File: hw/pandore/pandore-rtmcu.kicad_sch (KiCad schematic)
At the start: 0 parts

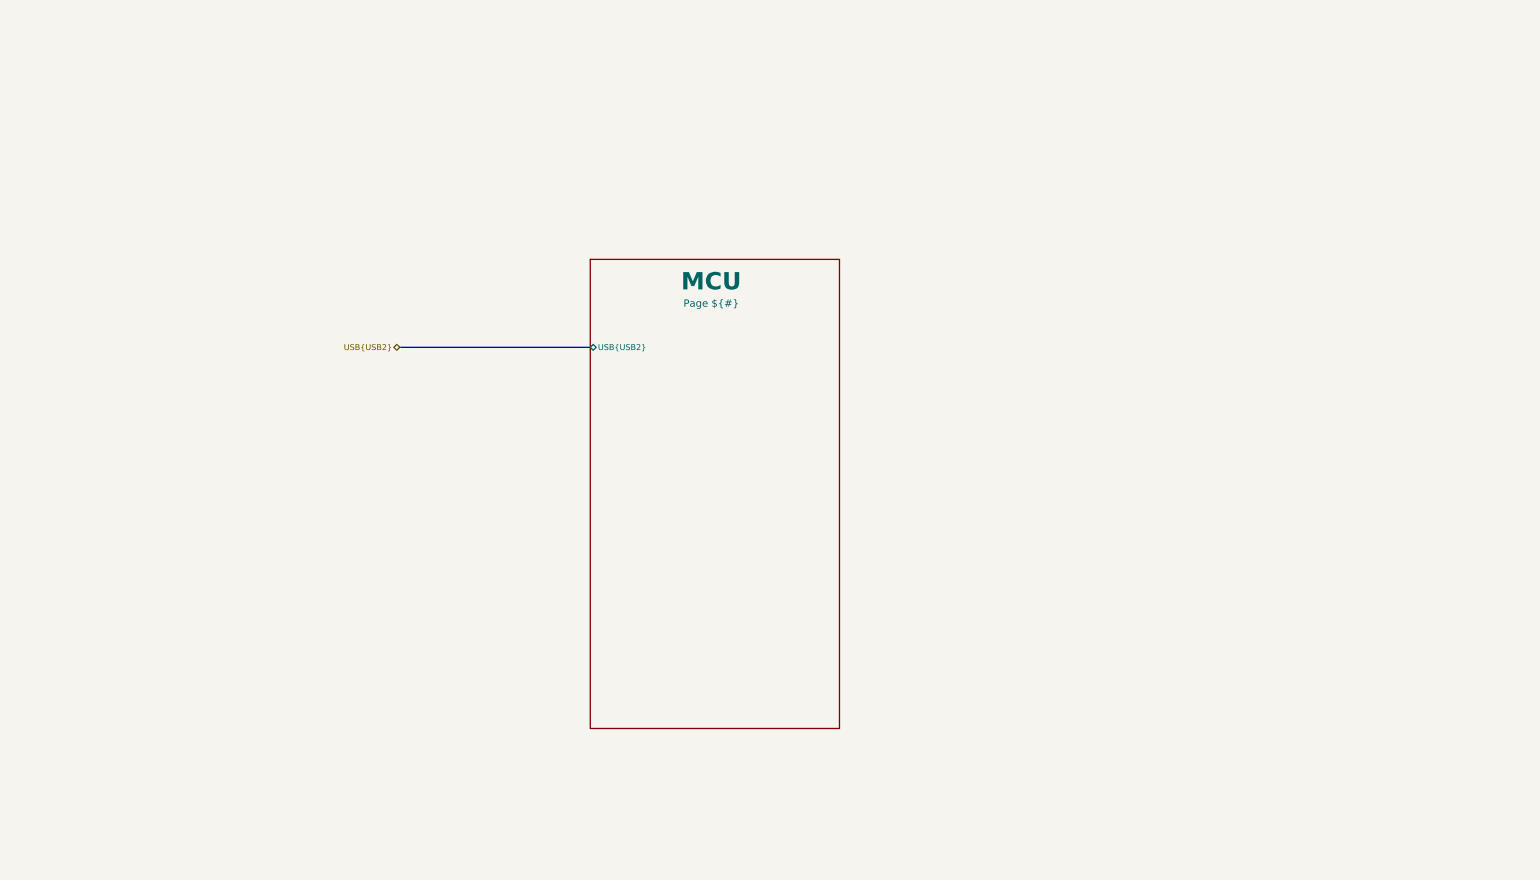
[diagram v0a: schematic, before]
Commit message: Added lots to sch and pcb: eth passive, audio codec, midi, teensy Corrected and added support for M.2
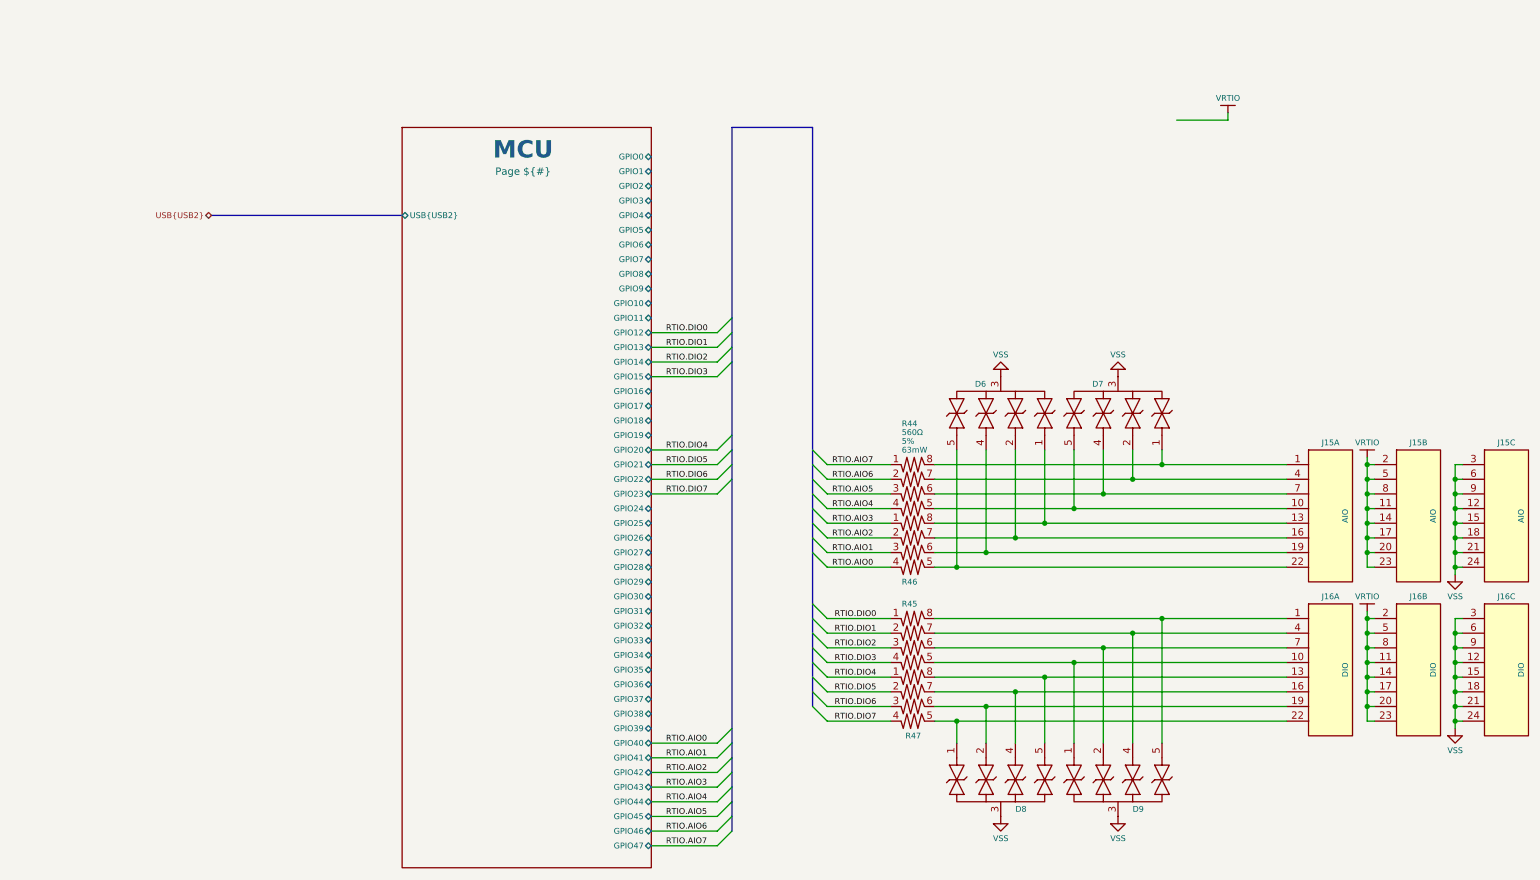
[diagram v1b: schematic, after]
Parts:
- added D6, D7, D8, D9: ${Vbr}, reekilib_dfn:DFN50P100X250X55-10, symbol reekilib_tvs:diode_tvsbi_4
- added J15: AIO, reekilib_con:HDR254P3X8-THRA, symbol reekilib_con:hdr-3x8
- added J16: DIO, reekilib_con:HDR254P3X8-THRA, symbol reekilib_con:hdr-3x8
- added R44, R45, R46, R47: ${Resistance}, ${Tolerance}, ${Power}, reekilib_res:RESCAXSR50P200X100X35-8, symbol reekilib_res:res_4
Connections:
- new net: D8.1, J16.22, R47.5
- new net: D8.2, J16.19, R47.6
- new net: D8.4, J16.16, R47.7
- new net: D8.5, J16.13, R47.8
- new net: D7.1, J15.1, R44.8
- new net: D7.5, J15.10, R44.5
- new net: D6.1, J15.13, R46.8
- new net: D6.2, J15.16, R46.7
- new net: D6.4, J15.19, R46.6
- new net: D6.5, J15.22, R46.5
- new net: D7.2, J15.4, R44.7
- new net: D7.4, J15.7, R44.6
- new net: D9.5, J16.1, R45.8
- new net: D9.1, J16.10, R45.5
- new net: D9.4, J16.4, R45.7
- new net: D9.2, J16.7, R45.6
- new net RTIO.AIO0: R46.4
- new net RTIO.AIO1: R46.3
- new net RTIO.AIO2: R46.2
- new net RTIO.AIO3: R46.1
- new net RTIO.AIO4: R44.4
- new net RTIO.AIO5: R44.3
- new net RTIO.AIO6: R44.2
- new net RTIO.AIO7: R44.1
- new net RTIO.DIO0: R45.1
- new net RTIO.DIO1: R45.2
- new net RTIO.DIO2: R45.3
- new net RTIO.DIO3: R45.4
- new net RTIO.DIO4: R47.1
- new net RTIO.DIO5: R47.2
- new net RTIO.DIO6: R47.3
- new net RTIO.DIO7: R47.4
- new net VRTIO: J15.11, J15.14, J15.17, J15.2, J15.20, J15.23, J15.5, J15.8, J16.11, J16.14, J16.17, J16.2, J16.20, J16.23, J16.5, J16.8
- new net VSS: D6.3, D7.3, D8.3, D9.3, J15.12, J15.15, J15.18, J15.21, J15.24, J15.3, J15.6, J15.9, J16.12, J16.15, J16.18, J16.21, J16.24, J16.3, J16.6, J16.9
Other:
- sheet MCU ports: added GPIO0, GPIO1, GPIO10, GPIO11, GPIO12, GPIO13, GPIO14, GPIO15, GPIO16, GPIO17, GPIO18, GPIO19, GPIO2, GPIO20, GPIO21, GPIO22, GPIO23, GPIO24, GPIO25, GPIO26, GPIO27, GPIO28, GPIO29, GPIO3, GPIO30, GPIO31, GPIO32, GPIO33, GPIO34, GPIO35, GPIO36, GPIO37, GPIO38, GPIO39, GPIO4, GPIO40, GPIO41, GPIO42, GPIO43, GPIO44, GPIO45, GPIO46, GPIO47, GPIO5, GPIO6, GPIO7, GPIO8, GPIO9; removed none

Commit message: Lots of routing done power blocks intra-routing mostly done rp2350 routing mostly done some label cleanup
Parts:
- D6, D7, D8, D9: footprint reekilib_dfn:DFN50P100X250X55-10 -> reekilib_dfn:DFN50P100X250X55-10_ESD204
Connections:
- net RTIO.DIO0: now also R47.4; no longer R45.1
- net RTIO.DIO1: now also R47.3; no longer R45.2
- net RTIO.DIO2: now also R47.2; no longer R45.3
- net RTIO.DIO3: now also R47.1; no longer R45.4
- net RTIO.DIO4: now also R45.4; no longer R47.1
- net RTIO.DIO5: now also R45.3; no longer R47.2
- net RTIO.DIO6: now also R45.2; no longer R47.3
- net RTIO.DIO7: now also R45.1; no longer R47.4
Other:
- sheet MCU ports: added VIO; removed none

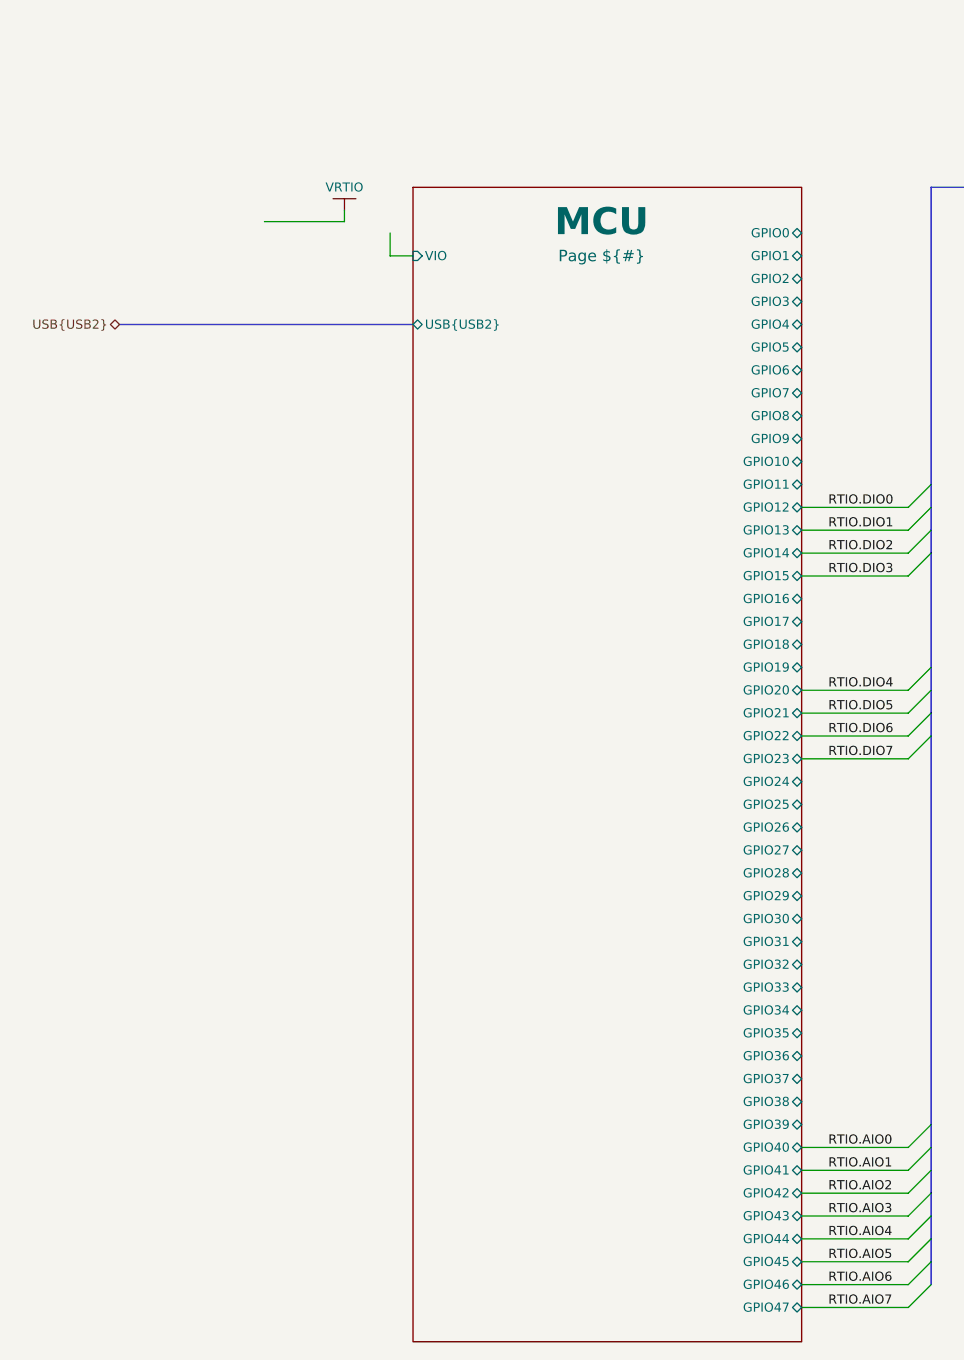
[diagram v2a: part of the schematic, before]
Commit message: added encoder, more routing done, pinout doc added
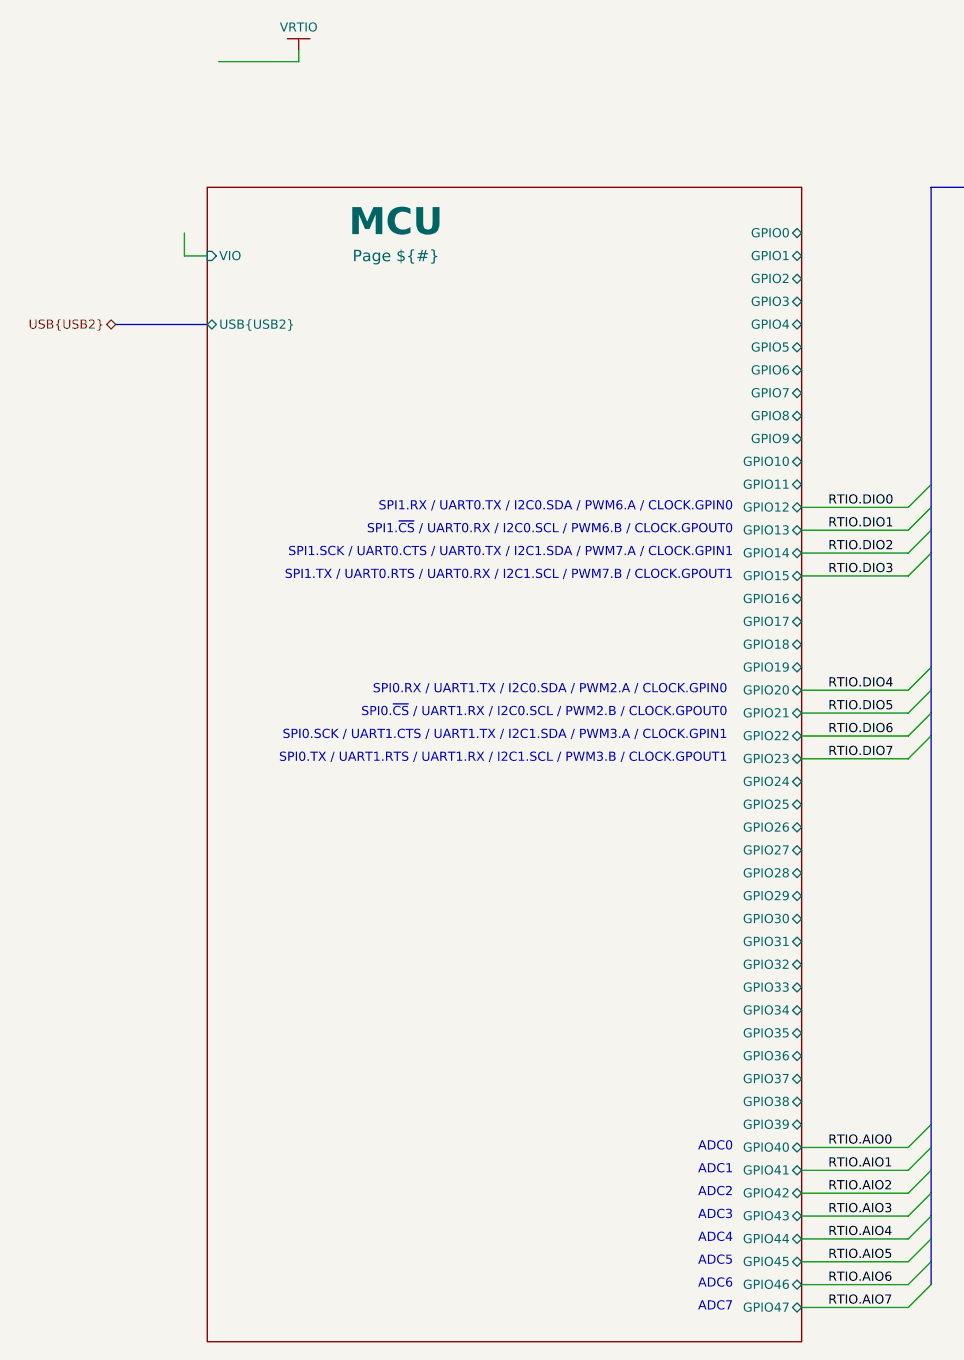
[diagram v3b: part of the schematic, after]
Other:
- note added: "ADC0"
- note added: "ADC1"
- note added: "ADC2"
- note added: "ADC3"
- note added: "ADC4"
- note added: "ADC5"
- note added: "ADC6"
- note added: "ADC7"
- note added: "SPI0.RX / UART1.TX / I2C0.SDA / PWM2.A / CLOCK.GPIN0"
- note added: "SPI0.SCK / UART1.CTS / UART1.TX / I2C1.SDA / PWM3.A / CLOCK.GPIN1"
- note added: "SPI0.TX / UART1.RTS / UART1.RX / I2C1.SCL / PWM3.B / CLOCK.GPOUT1"
- note added: "SPI0.~{CS} / UART1.RX / I2C0.SCL / PWM2.B / CLOCK.GPOUT0"
- note added: "SPI1.RX / UART0.TX / I2C0.SDA / PWM6.A / CLOCK.GPIN0"
- note added: "SPI1.SCK / UART0.CTS / UART0.TX / I2C1.SDA / PWM7.A / CLOCK.GPIN1"
- note added: "SPI1.TX / UART0.RTS / UART0.RX / I2C1.SCL / PWM7.B / CLOCK.GPOUT1"
- note added: "SPI1.~{CS} / UART0.RX / I2C0.SCL / PWM6.B / CLOCK.GPOUT0"
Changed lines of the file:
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@@
 		(company "${corp}")
 	)
+	(text "ADC1"
+		(exclude_from_sim no)
+		(at 121.92 147.32 0)
+		(effects
+			(font
+				(size 1.016 1.016)
+			)
+			(justify right)
+		)
+	)
+	(text "SPI0.~{CS} / UART1.RX / I2C0.SCL / PWM2.B / CLOCK.GPOUT0"
+		(exclude_from_sim no)
+		(at 121.285 96.52 0)
+		(effects
+			(font
+				(size 1.016 1.016)
+			)
+			(justify right)
+		)
+	)
+	(text "ADC6"
+		(exclude_from_sim no)
+		(at 121.92 160.02 0)
+		(effects
+			(font
+				(size 1.016 1.016)
+			)
+			(justify right)
+		)
+	)
+	(text "SPI0.RX / UART1.TX / I2C0.SDA / PWM2.A / CLOCK.GPIN0"
+		(exclude_from_sim no)
+		(at 121.285 93.98 0)
+		(effects
+			(font
+				(size 1.016 1.016)
+			)
+			(justify right)
+		)
+	)
+	(text "SPI1.SCK / UART0.CTS / UART0.TX / I2C1.SDA / PWM7.A / CLOCK.GPIN1"
+		(exclude_from_sim no)
+		(at 121.92 78.74 0)
+		(effects
+			(font
+				(size 1.016 1.016)
+			)
+			(justify right)
+		)
+	)
+	(text "SPI0.TX / UART1.RTS / UART1.RX / I2C1.SCL / PWM3.B / CLOCK.GPOUT1"
+		(exclude_from_sim no)
+		(at 121.285 101.6 0)
+		(effects
+			(font
+				(size 1.016 1.016)
+			)
+			(justify right)
+		)
+	)
+	(text "SPI1.~{CS} / UART0.RX / I2C0.SCL / PWM6.B / CLOCK.GPOUT0"
+		(exclude_from_sim no)
+		(at 121.92 76.2 0)
+		(effects
+			(font
+				(size 1.016 1.016)
+			)
+			(justify right)
+		)
+	)
+	(text "SPI0.SCK / UART1.CTS / UART1.TX / I2C1.SDA / PWM3.A / CLOCK.GPIN1"
+		(exclude_from_sim no)
+		(at 121.285 99.06 0)
+		(effects
+			(font
+				(size 1.016 1.016)
+			)
+			(justify right)
+		)
+	)
+	(text "SPI1.RX / UART0.TX / I2C0.SDA / PWM6.A / CLOCK.GPIN0"
+		(exclude_from_sim no)
+		(at 121.92 73.66 0)
+		(effects
+			(font
+				(size 1.016 1.016)
+			)
+			(justify right)
+		)
+	)
+	(text "SPI1.TX / UART0.RTS / UART0.RX / I2C1.SCL / PWM7.B / CLOCK.GPOUT1"
+		(exclude_from_sim no)
+		(at 121.92 81.28 0)
+		(effects
+			(font
+				(size 1.016 1.016)
+			)
+			(justify right)
+		)
+	)
+	(text "ADC3"
+		(exclude_from_sim no)
+		(at 121.92 152.4 0)
+		(effects
+			(font
+				(size 1.016 1.016)
+			)
+			(justify right)
+		)
+	)
+	(text "ADC0"
+		(exclude_from_sim no)
+		(at 121.92 144.78 0)
+		(effects
+			(font
+				(size 1.016 1.016)
+			)
+			(justify right)
+		)
+	)
+	(text "ADC4"
+		(exclude_from_sim no)
+		(at 121.92 154.94 0)
+		(effects
+			(font
+				(size 1.016 1.016)
+			)
+			(justify right)
+		)
+	)
+	(text "ADC2"
+		(exclude_from_sim no)
+		(at 121.92 149.86 0)
+		(effects
+			(font
+				(size 1.016 1.016)
+			)
+			(justify right)
+		)
+	)
+	(text "ADC5"
+		(exclude_from_sim no)
+		(at 121.92 157.48 0)
+		(effects
+			(font
+				(size 1.016 1.016)
+			)
+			(justify right)
+		)
+	)
+	(text "ADC7"
+		(exclude_from_sim no)
+		(at 121.92 162.56 0)
+		(effects
+			(font
+				(size 1.016 1.016)
+			)
+			(justify right)
+		)
+	)
 	(junction
 		(at 254 109.22)
@@
 		)
 	)
+	(bus
+		(pts
+			(xy 53.34 53.34) (xy 63.5 53.34)
+		)
+		(stroke
+			(width 0)
+			(type default)
+		)
+	)
 	(wire
 		(pts
@@
 	(wire
 		(pts
-			(xy 83.82 43.18) (xy 83.82 45.72)
+			(xy 60.96 43.18) (xy 60.96 45.72)
 		)
 		(stroke
@@
 	(bus
 		(pts
-			(xy 53.7563 53.34) (xy 86.36 53.34)
-		)
-		(stroke
-			(width 0)
-			(type default)
-		)
-	)
-	(bus
-		(pts
 			(xy 143.9263 96.52) (xy 143.9263 99.06)
 		)
@@
 	(wire
 		(pts
-			(xy 69.85 41.91) (xy 78.74 41.91)
+			(xy 64.77 24.13) (xy 73.66 24.13)
 		)
 		(stroke
@@
 	(wire
 		(pts
-			(xy 78.74 40.64) (xy 78.74 41.91)
+			(xy 73.66 22.86) (xy 73.66 24.13)
 		)
 		(stroke
@@
 	(wire
 		(pts
-			(xy 86.36 45.72) (xy 83.82 45.72)
+			(xy 63.5 45.72) (xy 60.96 45.72)
 		)
 		(stroke
@@
 	(hierarchical_label "USB{USB2}"
 		(shape bidirectional)
-		(at 53.7563 53.34 180)
+		(at 53.34 53.34 180)
 		(effects
 			(font
@@
 		(length 1.27)
 		(shape diamond)
-		(at 72.39 41.91 0)
+		(at 67.31 24.13 0)
 		(fields_autoplaced yes)
 		(effects
@@
 		)
 		(property "Netclass" "PWR"
-			(at 73.4873 40.64 0)
+			(at 68.4073 22.86 0)
 			(effects
 				(font
@@
 		)
 		(property "Component Class" ""
-			(at -101.6 5.08 0)
+			(at -106.68 -12.7 0)
 			(effects
 				(font
@@
 	(symbol
 		(lib_id "reekilib_pwr:VDD")
-		(at 78.74 39.37 0)
+		(at 73.66 21.59 0)
 		(unit 1)
 		(exclude_from_sim no)
@@
 		(dnp no)
 		(property "Reference" "#PWR063"
-			(at 78.74 36.195 0)
+			(at 73.66 18.415 0)
 			(do_not_autoplace yes)
 			(effects
@@
 		)
 		(property "Value" "VRTIO"
-			(at 78.74 38.1 0)
+			(at 73.66 20.32 0)
 			(effects
 				(font
@@
 		)
 		(property "Footprint" ""
-			(at 78.74 39.37 0)
+			(at 73.66 21.59 0)
 			(effects
 				(font
@@
 		)
 		(property "Datasheet" ""
-			(at 78.74 39.37 0)
+			(at 73.66 21.59 0)
 			(effects
 				(font
@@
 		)
 		(property "Description" ""
-			(at 78.74 39.37 0)
+			(at 73.66 21.59 0)
 			(effects
 				(font
@@
 	)
 	(sheet
-		(at 86.36 38.1)
-		(size 43.18 128.27)
+		(at 63.5 38.1)
+		(size 66.04 128.27)
 		(exclude_from_sim no)
 		(in_bom yes)
@@
 		)
 		(property "Sheetname" "MCU"
-			(at 107.315 41.91 0)
+			(at 84.455 41.91 0)
 			(do_not_autoplace yes)
 			(effects
@@
 		)
 		(property "Sheetfile" "pandore-mcu.kicad_sch"
-			(at 86.868 75.692 0)
+			(at 64.008 75.692 0)
 			(effects
 				(font
@@
 		)
 		(property "pageNb" "Page ${#}"
-			(at 107.315 45.72 0)
+			(at 84.455 45.72 0)
 			(effects
 				(font
@@
 		)
 		(pin "USB{USB2}" bidirectional
-			(at 86.36 53.34 180)
+			(at 63.5 53.34 180)
 			(effects
 				(font
@@
 		)
 		(pin "VIO" input
-			(at 86.36 45.72 180)
+			(at 63.5 45.72 180)
 			(effects
 				(font

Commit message: added todos following review
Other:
- note added: "TODO: RTIO Voltage choice: 3.3V"
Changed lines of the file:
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@@
+		)
+	)
+	(text "TODO: RTIO Voltage choice: 3.3V"
+		(exclude_from_sim no)
+		(at 243.586 82.55 0)
+		(effects
+			(font
+				(size 1.016 1.016)
+			)
 		)
 	)

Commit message: most of board control signals added, routed and defined
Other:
- sheet MCU ports: added ~{RST}, ~{USBBOOT}; removed none
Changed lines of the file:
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@@
 	)
 	(bus_entry
+		(at 48.26 54.61)
+		(size 2.54 2.54)
+		(stroke
+			(width 0)
+			(type default)
+		)
+	)
+	(bus_entry
 		(at 157.8963 128.27)
 		(size 2.54 2.54)
@@
 	)
 	(bus_entry
+		(at 48.26 57.15)
+		(size 2.54 2.54)
+		(stroke
+			(width 0)
+			(type default)
+		)
+	)
+	(bus_entry
 		(at 157.8963 123.19)
 		(size 2.54 2.54)
@@
 	(bus
 		(pts
-			(xy 53.34 53.34) (xy 63.5 53.34)
+			(xy 46.99 52.07) (xy 63.5 52.07)
 		)
 		(stroke
@@
 		)
 	)
+	(bus
+		(pts
+			(xy 48.26 54.61) (xy 48.26 57.15)
+		)
+		(stroke
+			(width 0)
+			(type default)
+		)
+	)
 	(wire
 		(pts
@@
 		)
 	)
+	(bus
+		(pts
+			(xy 46.99 54.61) (xy 48.26 54.61)
+		)
+		(stroke
+			(width 0)
+			(type default)
+		)
+	)
 	(wire
 		(pts
@@
 	(wire
 		(pts
+			(xy 50.8 59.69) (xy 63.5 59.69)
+		)
+		(stroke
+			(width 0)
+			(type default)
+		)
+	)
+	(wire
+		(pts
 			(xy 269.24 125.73) (xy 269.24 128.27)
 		)
@@
 		)
 	)
+	(wire
+		(pts
+			(xy 50.8 57.15) (xy 63.5 57.15)
+		)
+		(stroke
+			(width 0)
+			(type default)
+		)
+	)
 	(bus
 		(pts
@@
 		)
 	)
+	(label "CTL.~{USBBOOT}"
+		(at 52.07 59.69 0)
+		(effects
+			(font
+				(size 1.016 1.016)
+			)
+			(justify left bottom)
+		)
+	)
 	(label "RTIO.AIO3"
 		(at 132.4963 152.4 0)
@@
 		)
 	)
+	(label "CTL.~{RST}"
+		(at 52.07 57.15 0)
+		(effects
+			(font
+				(size 1.016 1.016)
+			)
+			(justify left bottom)
+		)
+	)
 	(label "RTIO.AIO7"
 		(at 161.29 96.52 0)
@@
 	(hierarchical_label "USB{USB2}"
 		(shape bidirectional)
-		(at 53.34 53.34 180)
+		(at 46.99 52.07 180)
+		(effects
+			(font
+				(size 1.016 1.016)
+			)
+			(justify right)
+		)
+	)
+	(hierarchical_label "CTL{~{RST} ~{USBBOOT}}"
+		(shape input)
+		(at 46.99 54.61 180)
 		(effects
 			(font
@@
 		)
 		(pin "USB{USB2}" bidirectional
-			(at 63.5 53.34 180)
+			(at 63.5 52.07 180)
 			(effects
 				(font
@@
 			(effects
 				(font
+					(size 1.016 1.016)
+				)
+				(justify left)
+			)
+		)
+		(pin "~{USBBOOT}" input
+			(at 63.5 59.69 180)
+			(effects
+				(font
+					(size 1.016 1.016)
+				)
+				(justify left)
+			)
+		)
+		(pin "~{RST}" input
+			(at 63.5 57.15 180)
+			(effects
+				(font

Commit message: added expansion port and more ctl to rp2350s routing much progress
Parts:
- added B4: mom_tact_no, reekilib_msw:tact_460X320X250, symbol reekilib_msw:mom_tact_no
- added JMP14: USBBOOT, reekilib_con:HDR254P1X02-TH, symbol reekilib_con:hdr-1x2
- added R243, R244: ${Resistance}, ${Tolerance}, ${Power}, reekilib_res:RESC1005, symbol reekilib_res:res
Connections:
- net CTL.~{RST}: now also R243.2
- net CTL.~{USBBOOT}: now also R244.2
- net VSS: now also B4.1, B4.2, JMP14.1
- new net: JMP14.2, R244.1
- new net: B4.3, B4.4, R243.1
